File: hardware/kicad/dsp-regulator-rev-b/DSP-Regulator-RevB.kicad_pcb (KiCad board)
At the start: 2 copper layers, 100 x 100 mm, 97 parts, among them J1 CLP-110-02-X-D, J2 CLP-110-02-X-D, J3 1935161, J4 Wire con, J5 Wire con, Q1 BSS138, Q16 BSS138, Q3 BSS138, Q4 BSS138, U2 LM2596S-ADJ, U3 LM2596S-ADJ, U4 LM2596S-ADJ, U5 LMV358IDR, U6 LMV358IDR

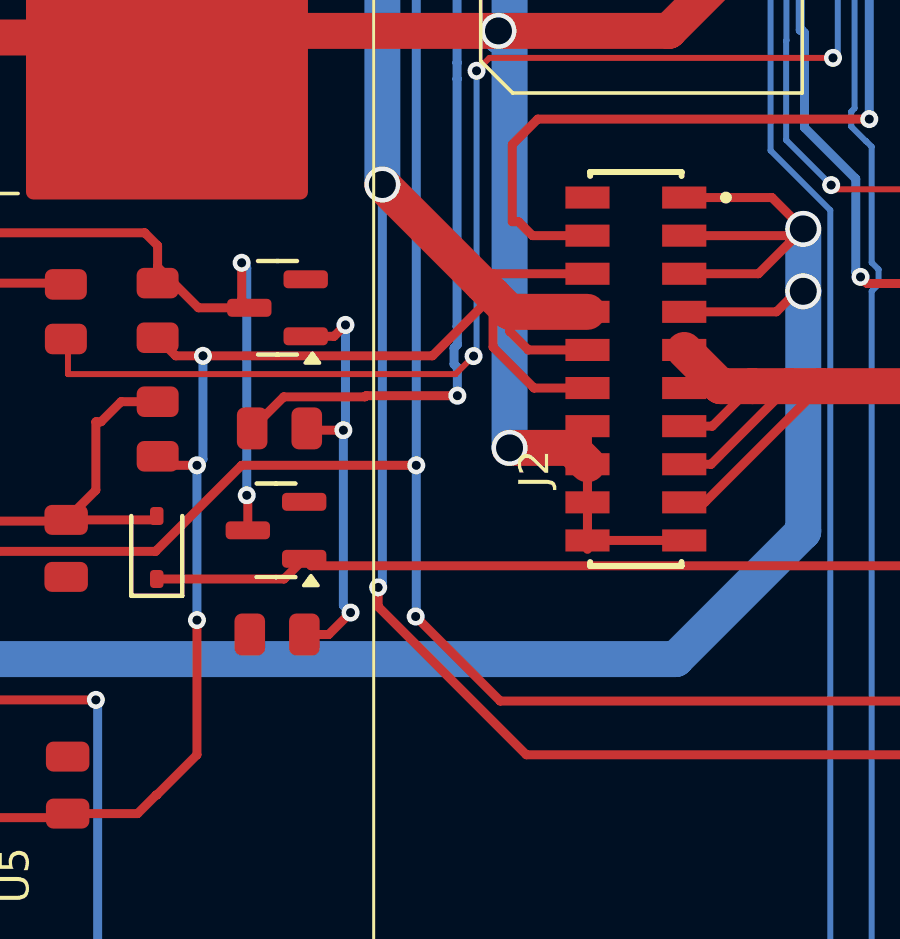
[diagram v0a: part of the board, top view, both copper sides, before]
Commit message: Capture VSENSE selector issue, SPICE validation, and pre-RevC routing blocker
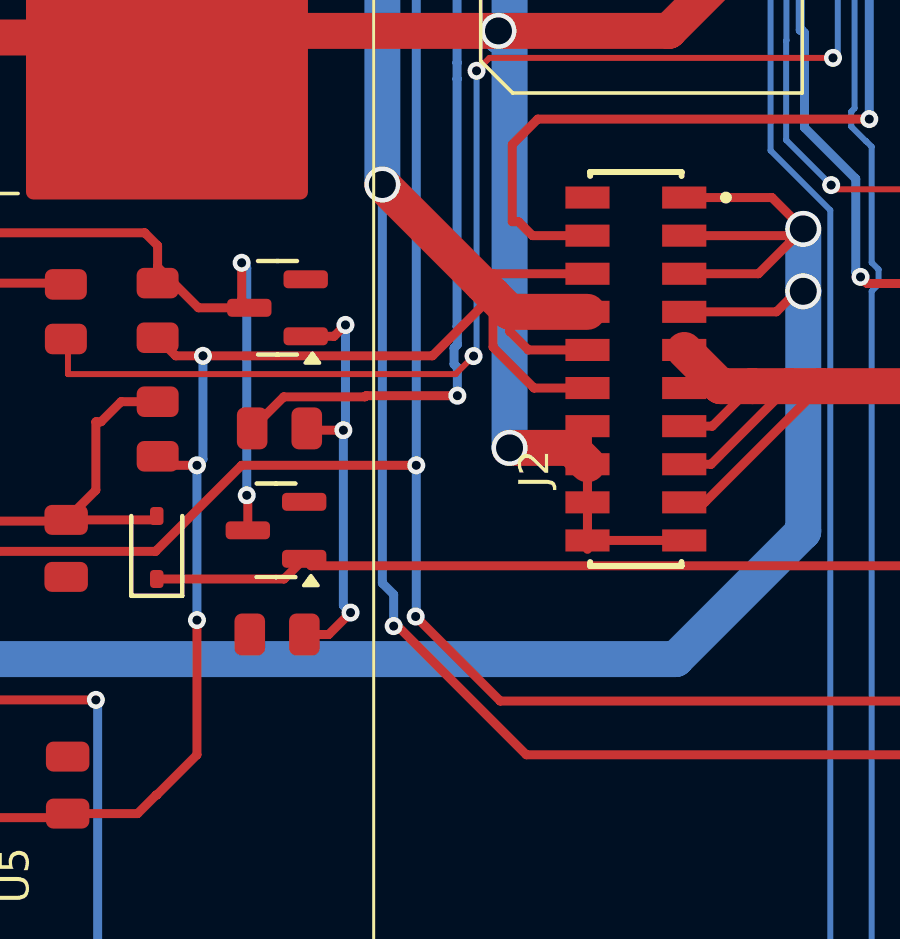
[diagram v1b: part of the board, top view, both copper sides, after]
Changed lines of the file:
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@@
 	)
 	(segment
+		(start 177.499 133.97)
+		(end 181.789 138.26)
+		(width 0.3)
+		(layer "F.Cu")
+		(net 3)
+	)
+	(segment
 		(start 183.8271 122.225)
 		(end 183.827 122.225)
@@
 	)
 	(segment
-		(start 158.75 94.32)
-		(end 163.13 94.32)
-		(width 1.2)
+		(start 177.366787 133.97)
+		(end 177.499 133.97)
+		(width 0.3)
 		(layer "F.Cu")
 		(net 3)
 	)
 	(segment
-		(start 181.789 138.26)
-		(end 210.06 138.26)
-		(width 0.3)
+		(start 158.75 94.32)
+		(end 163.13 94.32)
+		(width 1.2)
 		(layer "F.Cu")
 		(net 3)
@@
 	)
 	(segment
-		(start 176.85 132.68)
-		(end 176.85 133.321)
-		(width 0.3)
-		(layer "F.Cu")
-		(net 3)
-	)
-	(segment
 		(start 156.66 91.42)
 		(end 158.75 93.51)
@@
 	)
 	(segment
-		(start 176.85 133.321)
-		(end 181.789 138.26)
-		(width 0.3)
-		(layer "F.Cu")
-		(net 3)
-	)
-	(segment
 		(start 181.855 124.765)
 		(end 181.235 124.145)
@@
 	)
 	(segment
+		(start 181.789 138.26)
+		(end 210.06 138.26)
+		(width 0.3)
+		(layer "F.Cu")
+		(net 3)
+	)
+	(segment
 		(start 159.74 87.86)
 		(end 159.68 87.92)
@@
 	)
 	(via
-		(at 176.85 132.68)
+		(at 177.366787 133.97)
 		(size 0.6)
 		(drill 0.3)
@@
 	)
 	(segment
-		(start 176.99 132.54)
-		(end 176.85 132.68)
-		(width 0.3)
-		(layer "B.Cu")
-		(net 3)
-	)
-	(segment
 		(start 171.01 128.41)
 		(end 170.81 128.61)
@@
 	)
 	(segment
+		(start 176.99 132.54)
+		(end 176.99 119.25)
+		(width 0.3)
+		(layer "B.Cu")
+		(net 3)
+	)
+	(segment
 		(start 171.01 124.961)
 		(end 171.01 128.41)
@@
 	)
 	(segment
-		(start 176.99 119.25)
+		(start 177.366787 132.916787)
 		(end 176.99 132.54)
 		(width 0.3)
@@
 	)
 	(segment
+		(start 177.366787 133.97)
+		(end 177.366787 132.916787)
+		(width 0.3)
+		(layer "B.Cu")
+		(net 3)
+	)
+	(segment
 		(start 208.68 134.37)
 		(end 214.59 134.37)
@@
 		(min_thickness 0.25)
 		(filled_areas_thickness no)
-		(fill yes
+		(fill
 			(thermal_gap 0.5)
 			(thermal_bridge_width 0.5)
